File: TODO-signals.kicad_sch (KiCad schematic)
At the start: 0 parts

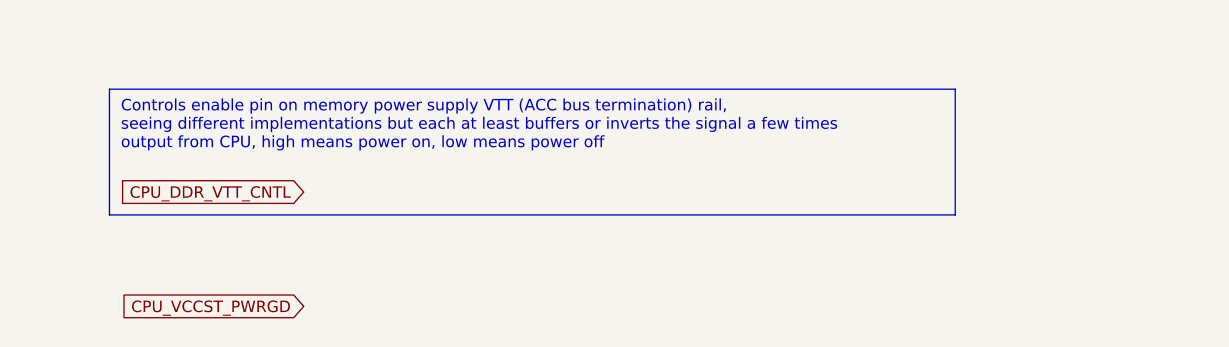
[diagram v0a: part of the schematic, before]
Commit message: Restructured schematic
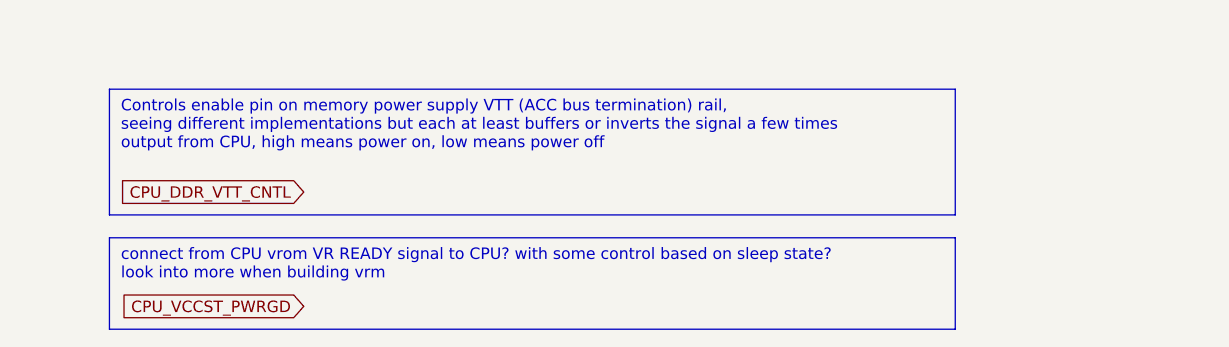
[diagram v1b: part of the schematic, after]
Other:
- note added: "connect from CPU vrom VR READY signal to CPU? with some control based on sleep state? look into more when building vrm"
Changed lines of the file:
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@@
+	)
+	(rectangle
+		(start 20.32 39.37)
+		(end 114.3 49.53)
+		(stroke
+			(width 0)
+			(type default)
+		)
+		(fill
+			(type none)
+		)
 	)
 	(rectangle
@@
 		)
 	)
+	(text "connect from CPU vrom VR READY signal to CPU? with some control based on sleep state?\nlook into more when building vrm"
+		(exclude_from_sim no)
+		(at 21.59 40.64 0)
+		(effects
+			(font
+				(size 1.27 1.27)
+			)
+			(justify left top)
+		)
+	)
